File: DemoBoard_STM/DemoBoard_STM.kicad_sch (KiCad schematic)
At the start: 56 parts, among them J1 USB4110GFA, J6 M55-7101242R, J7 MSD-1-A, J8 Conn_01x17_Pin, SW1 SW_Push, SW2 SW_Push, U1 RP2040, U2 W25Q128JVSIM, U3 MCP2518FDT-E_QBB, U4 TCAN332DCNR, U5 TLV75533PDBVR, Y1 ABM8-272-T3, Y2 ABM8-20.000MHZ-10-B1U-T

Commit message: Implement STM schematic
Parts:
- removed C1, C2: 15pF, Capacitor_SMD:C_0402_1005Metric_Pad0.74x0.62mm_HandSolder, symbol Device:C
- removed C10, C11, C13, C4, C5, C6, C7, C8: 100nF, Capacitor_SMD:C_0402_1005Metric_Pad0.74x0.62mm_HandSolder, symbol Device:C
- removed C3, C9: 1uF, Capacitor_SMD:C_0402_1005Metric_Pad0.74x0.62mm_HandSolder, symbol Device:C
- removed R2, R4: 27.4, Resistor_SMD:R_0402_1005Metric_Pad0.72x0.64mm_HandSolder, symbol Device:R_US
- removed R3: 10k, Resistor_SMD:R_0402_1005Metric_Pad0.72x0.64mm_HandSolder, symbol Device:R_US
- removed R5: 1k, Resistor_SMD:R_0402_1005Metric_Pad0.72x0.64mm_HandSolder, symbol Device:R_US
- removed TP1: 1.2V, TestPoint:TestPoint_Pad_D1.0mm, symbol Connector:TestPoint
- removed TP3: 3.3V, TestPoint:TestPoint_Pad_D1.0mm, symbol Connector:TestPoint
- removed U1: RP2040, Package_DFN_QFN:QFN-56-1EP_7x7mm_P0.4mm_EP3.2x3.2mm, symbol MCU_RaspberryPi:RP2040
- removed Y1: ABM8-272-T3, inspireFly:XTAL_ABM8-272-T3, symbol inspireFly:ABM8-272-T3
- added C26, C40: 1uF, Capacitor_SMD:C_0402_1005Metric_Pad0.74x0.62mm_HandSolder, symbol Device:C
- added C27, C28, C29, C31, C35, C36, C37, C38, C39, C41: 100nF, Capacitor_SMD:C_0402_1005Metric_Pad0.74x0.62mm_HandSolder, symbol Device:C
- added C30, C32: 10uF, Capacitor_SMD:C_0402_1005Metric_Pad0.74x0.62mm_HandSolder, symbol Device:C
- added C33, C34: 2.2uF, Capacitor_SMD:C_0402_1005Metric_Pad0.74x0.62mm_HandSolder, symbol Device:C
- added D3: PESD3V3U1UL, Diode_SMD:D_SOD-882, symbol Diode:PESD3V3U1UL
- added D4, D5: ESDA14V2SC5, Package_TO_SOT_SMD:SOT-23-5, symbol Power_Protection:ESDA14V2SC5
- added J2: Conn_ST_STDC14, symbol Connector:Conn_ST_STDC14
- added L1: 2.2uH, Inductor_SMD:L_0402_1005Metric_Pad0.77x0.64mm_HandSolder, symbol Device:L
- added U1: STM32U375CGT6Q, inspireFly:LQFP48_STM, symbol STM32U375:STM32U375CGT6Q
- added Y1: 32.768kHz, Crystal:Crystal_SMD_2012-2Pin_2.0x1.2mm_HandSoldering, symbol Device:Crystal
- added Y3: 16MHz, Crystal:Crystal_SMD_3225-4Pin_3.2x2.5mm_HandSoldering, symbol Device:Crystal_GND24
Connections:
- net RESET is gone; now on net COVER_GND: SW1.1
- net COVER_GND: now also C26.1, C27.1, C28.1, C29.1, C30.1, C31.1, C32.2, C33.1, C34.2, C35.2, C36.1, C37.2, C38.2, C39.2, C40.2, C41.1, D3.2 (A), D4.2 (A), D5.2 (A), J2.11 (GNDDetect), J2.5 (GND), J2.7 (GND), J2.9 (JRCLK/NC), U1.22 (VSSSMPS), U1.24 (VSS), U1.35 (VSS), U1.47 (VSS), U1.8 (VSSA), Y3.2 (G), Y3.4 (G); no longer SW1.2
- new net: C37.1, U1.6 (PH1-OSC_OUT), Y3.1
- new net: D4.5 (K), J2.10 (JTDI/NC), U1.38 (PA15)
- new net: C41.2, D3.1 (K), D5.1 (K), J2.12 (~{RST}), SW1.2, U1.7 (NRST)
- new net: D5.5 (K), J2.13 (VCP_RX), U1.31 (PA10)
- new net: D5.4 (K), J2.14 (VCP_TX), U1.30 (PA9)
- new net: D4.1 (K), J2.4 (JTMS/SWDIO), U1.34 (PA13)
- new net: D4.3 (K), J2.6 (JCLK/SWCLK), U1.37 (PA14)
- new net: D4.4 (K), J2.8 (JTDO/SWO), U1.39 (PB3)
- new net: L1.1, U1.20 (VLXSMPS)
- new net: C33.2, C34.1, L1.2, U1.23 (VDD11), U1.46 (VDD11)
- new net: C38.1, U1.5 (PH0-OSC_IN), Y3.3
- new net: C35.1, U1.3 (PC14-OSC32_IN), Y1.2
- new net: C36.2, U1.4 (PC15-OSC32_OUT), Y1.1
- new net PA0: U1.10 (PA0)
- new net PA1: U1.11 (PA1)
- new net PA11: U1.32 (PA11)
- new net PA12: U1.33 (PA12)
- new net PA2: U1.12 (PA2)
- new net PA3: U1.13 (PA3)
- new net PA4: U1.14 (PA4)
- new net PA5: U1.15 (PA5)
- new net PA6: U1.16 (PA6)
- new net PA7: U1.17 (PA7)
- new net PA8: U1.29 (PA8)
- new net PB0: U1.18 (PB0)
- new net PB1: U1.19 (PB1)
- new net PB13: U1.26 (PB13)
- new net PB14: U1.27 (PB14)
- new net PB15: U1.28 (PB15)
- new net PB4: U1.40 (PB4)
- new net PB5: U1.41 (PB5)
- new net PB6: U1.42 (PB6)
- new net PB7: U1.43 (PB7)
- new net PB8: U1.45 (PB8)
- new net PC13: U1.2 (PC13)
- new net PH3-BOOT0: U1.44 (PH3-BOOT0)
- new net VBAT: C26.2, U1.1 (VBAT)
- new net VCC: J2.3 (VCC)
- new net VDD: C27.2, C28.2, C29.2, C30.2, C31.2, C32.1, U1.21 (VDDSMPS), U1.25 (VDD), U1.36 (VDD), U1.48 (VDD)
- new net VDDA: C39.1, C40.1, U1.9 (VDDA)
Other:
- note added: "STM32U375CGT6Q"
- note removed: "Ground unused ADC pins"
- note removed: "Integration References: https://pip-assets.raspberrypi.com/categories/814-rp2040/documents/RP-008279-DS-1-hardware-design-with-rp2040.pdf?disposition=inline https://pip-assets.raspberrypi.com/categories/610-raspberry-pi-pico/documents/RP-008307-DS-1-pico-datasheet.pdf?disposition=inline#pico-schematic-diagram"
- note removed: "Place 27.4 ohm near respective pins"
- note removed: "Place C3/1uF near pin 45"
- note removed: "Place C9/1uF near pin 44"
- note removed: "RP2040"

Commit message: Fix cap values for clock
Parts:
- C35, C36: value 100nF -> 6.8pF
- C37, C38: value 100nF -> 12pF
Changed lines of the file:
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@@
 			)
 		)
-		(property "Value" "100nF"
+		(property "Value" "12pF"
 			(at 173.99 60.706 0)
 			(show_name no)
@@
 			)
 		)
-		(property "Value" "100nF"
+		(property "Value" "6.8pF"
 			(at 172.72 43.434 0)
 			(show_name no)
@@
 			)
 		)
-		(property "Value" "100nF"
+		(property "Value" "6.8pF"
 			(at 175.26 27.686 0)
 			(show_name no)
@@
 			)
 		)
-		(property "Value" "100nF"
+		(property "Value" "12pF"
 			(at 162.56 50.546 0)
 			(show_name no)

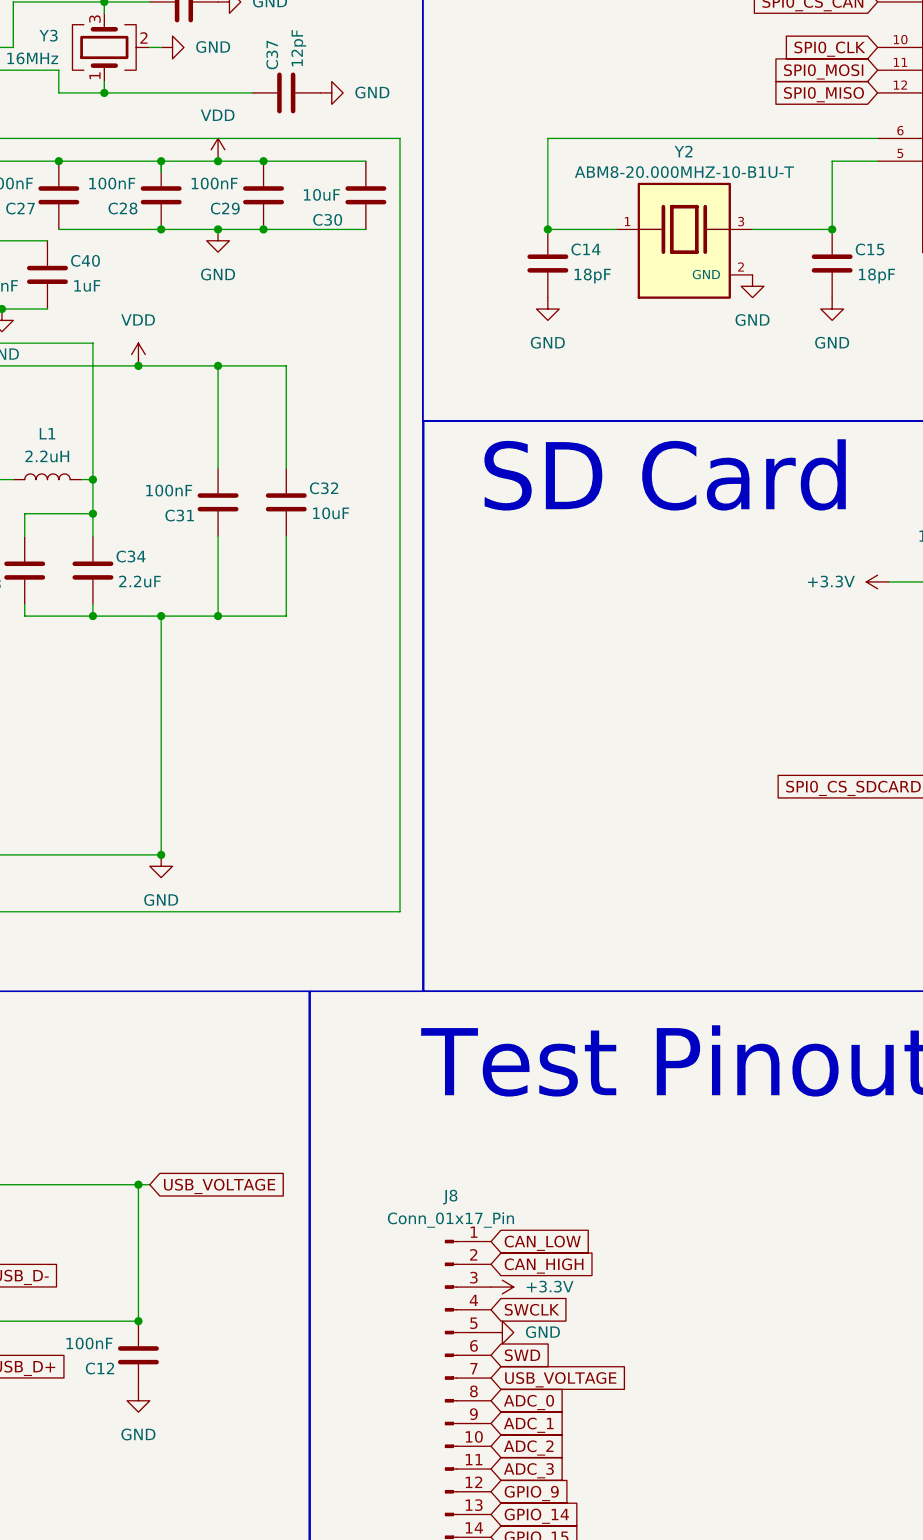
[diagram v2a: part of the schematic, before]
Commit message: Routed capacitors
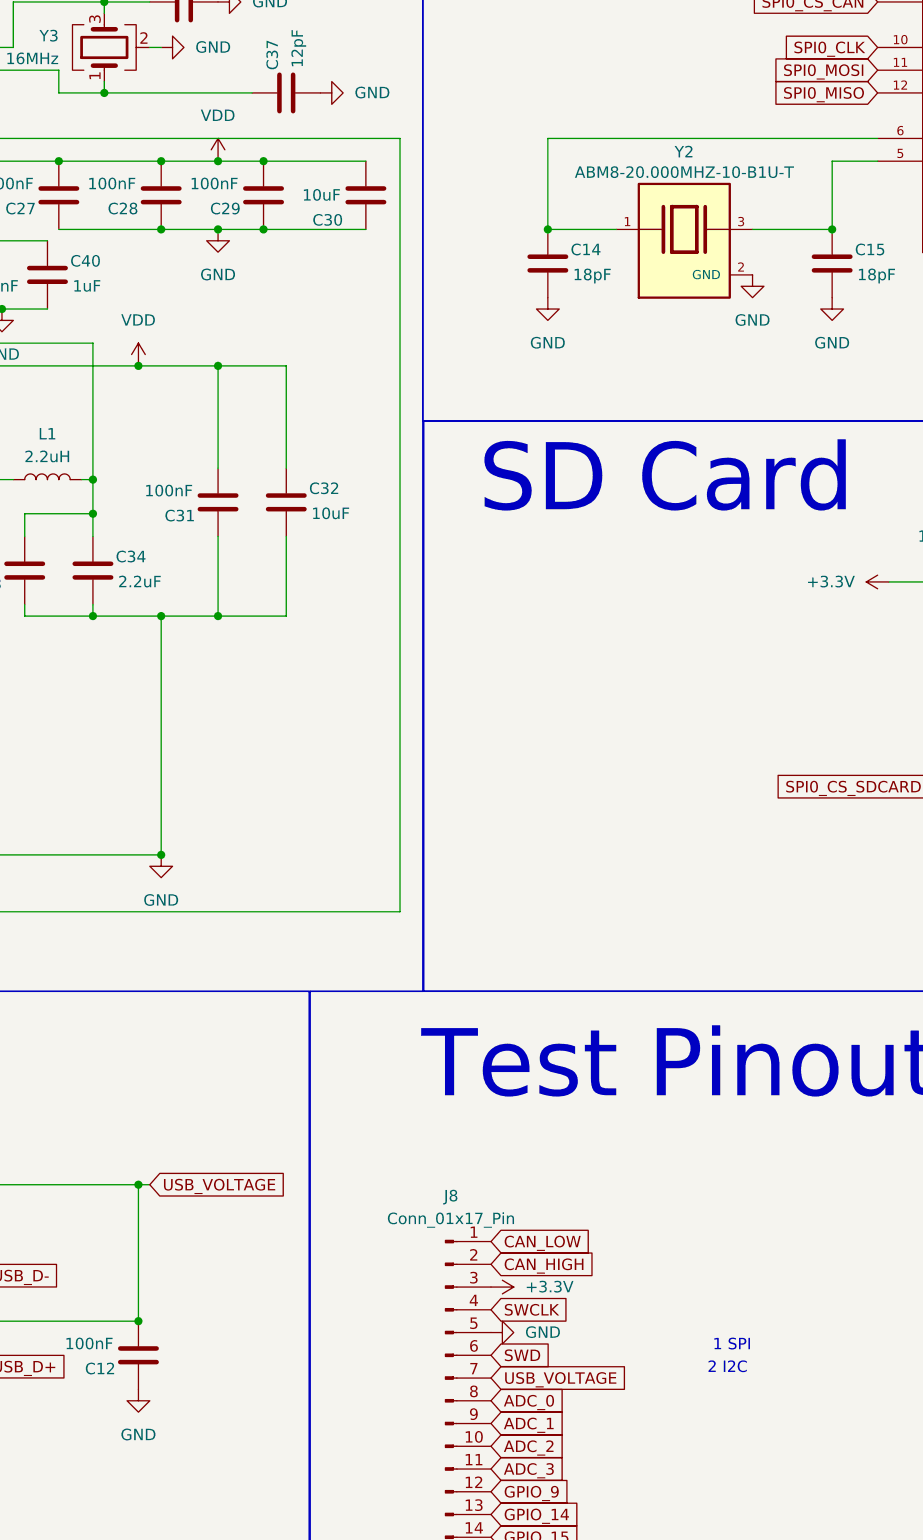
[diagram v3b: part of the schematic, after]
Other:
- note added: "1 SPI"
- note added: "2 I2C"

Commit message: Routing + schematic updates for STM
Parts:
- removed C12, C17, C41: 100nF, Capacitor_SMD:C_0402_1005Metric_Pad0.74x0.62mm_HandSolder, symbol Device:C
- removed C14, C15: 18pF, Capacitor_SMD:C_0402_1005Metric_Pad0.74x0.62mm_HandSolder, symbol Device:C
- removed C26: 1uF, Capacitor_SMD:C_0402_1005Metric_Pad0.74x0.62mm_HandSolder, symbol Device:C
- removed CR1: USBLC6-2SC6, Package_TO_SOT_SMD:SOT-23-6, symbol inspireFly:USBLC6-2SC6
- removed D1: LTST-C190KSKT, LED_SMD:LED_0603_1608Metric_Pad1.05x0.95mm_HandSolder, symbol Device:LED
- removed D2: LTST-S270KRKT, LED_SMD:LED_0603_1608Metric_Pad1.05x0.95mm_HandSolder, symbol Device:LED
- removed D3: PESD3V3U1UL, Diode_SMD:D_SOD-882, symbol Diode:PESD3V3U1UL
- removed D4, D5: ESDA14V2SC5, Package_TO_SOT_SMD:SOT-23-5, symbol Power_Protection:ESDA14V2SC5
- removed R8, R9: 1k, Resistor_SMD:R_0402_1005Metric_Pad0.72x0.64mm_HandSolder, symbol Device:R_US
- removed U2: W25Q128JVSIM, inspireFly:SOIC_128JVSIM_WIN, symbol inspireFly:W25Q128JVSIM
- removed U3: MCP2518FDT-E_QBB, inspireFly:SON65P450X300X90-15N, symbol inspireFly:MCP2518FDT-E_QBB
- removed Y2: ABM8-20.000MHZ-10-B1U-T, inspireFly:XTAL_ABM8-272-T3, symbol inspireFly:ABM8-272-T3
- removed Y3: 16MHz, Crystal:Crystal_SMD_3225-4Pin_3.2x2.5mm_HandSoldering, symbol Device:Crystal_GND24
- added CR1, CR2: ESDA14V2SC6, inspireFly:SOT23-6_1P75X3P05X0P95_STM, symbol inspireFly:ESDA14V2SC6
- added R12: 10k, Resistor_SMD:R_0402_1005Metric_Pad0.72x0.64mm_HandSolder, symbol Device:R_US
- added R13: 100k, Resistor_SMD:R_0402_1005Metric_Pad0.72x0.64mm_HandSolder, symbol Device:R_US
- added U3: W25Q128JVPIQ TR, inspireFly:WSON-8_6X5_WIN, symbol inspireFly:W25Q128JVPIQ_TR
- added Y2: 8Z-16.000MAHE-T, Crystal:Crystal_SMD_2520-4Pin_2.5x2.0mm, symbol Device:Crystal_GND24
- C35, C36: value 6.8pF -> 22pF
- C37, C38: value 12pF -> 18pF
- J2: footprint (none) -> inspireFly:SAMTEC_FTSH-107-01-L-DV-K-A
- L1: footprint Inductor_SMD:L_0402_1005Metric_Pad0.77x0.64mm_HandSolder -> inspireFly:INDC1608X95N
- Y1: footprint Crystal:Crystal_SMD_2012-2Pin_2.0x1.2mm_HandSoldering -> inspireFly:XTAL_ABS07-32.768KHZ-T
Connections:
- net GPIO_16 is gone; now on net CAN_HIGH: J8.15 (Pin_15)
- net GPIO_17 is gone; now on net CAN_LOW: J8.16 (Pin_16)
- net PA11 is gone; now on net CAN_RX: U1.32 (PA11)
- net PA12 is gone; now on net CAN_TX: U1.33 (PA12)
- net PA2 is gone; now on net QSPI_CS: U1.12 (PA2)
- net PA3 is gone; now on net QSPI_CLK: U1.13 (PA3)
- net PA6 is gone; now on net QSPI_SD3: U1.16 (PA6)
- net PA7 is gone; now on net QSPI_SD2: U1.17 (PA7)
- net PA8 is gone; now on net SPI2_CS2: U1.29 (PA8)
- net PB0 is gone; now on net QSPI_SD1: U1.18 (PB0)
- net PB1 is gone; now on net QSPI_SD0: U1.19 (PB1)
- net PB13 is gone; now on net SPI2_CLK: U1.26 (PB13)
- net PB14 is gone; now on net SPI2_MISO: U1.27 (PB14)
- net PB15 is gone; now on net SPI2_MOSI: U1.28 (PB15)
- net PB6 is gone; now on net I2C1_SCL: U1.42 (PB6)
- net PB7 is gone; now on net I2C1_SDA: U1.43 (PB7)
- net PB8 is gone; now on net SPI2_CS1: U1.45 (PB8)
- net SPI0_CLK is gone; now on net SPI1_CLK: J7.5 (CLK)
- net SPI0_CS_SDCARD is gone; now on net SPI1_CS_SDCARD: J7.2 (CD/DAT3), R11.2
- net SPI0_MISO is gone; now on net SPI1_MISO: J7.7 (DAT0)
- net SPI0_MOSI is gone; now on net SPI1_MOSI: J7.3 (CMD)
- net SWCLK is gone; now on net COVER_GND: J8.4 (Pin_4)
- net SWD is gone; now on net ADC1_IN4: J8.6 (Pin_6)
- net VBAT is gone; now on net +3.3V: U1.1 (VBAT)
- net VCC is gone; now on net +3.3V: J2.3 (VCC)
- net VDD is gone; now on net +3.3V: C27.2, C28.2, C29.2, C30.2, C31.2, C32.1, U1.21 (VDDSMPS), U1.25 (VDD), U1.36 (VDD), U1.48 (VDD)
- net VDDA is gone; now on net +3.3V: C39.1, C40.1, U1.9 (VDDA)
- net +3.3V: now also J8.1 (Pin_1), J8.2 (Pin_2), R7.2, SW2.2, CR1.1, R12.1, U3.8 (VCC); no longer J8.3 (Pin_3)
- net CAN_HIGH: no longer J8.2 (Pin_2)
- net CAN_LOW: no longer J8.1 (Pin_1)
- net COVER_GND: now also C38.1, J8.3 (Pin_3), CR1.2, CR1.5, CR2.2, CR2.5, R13.2, U3.4 (GND), U3.9 (GND), Y2.2 (G), Y2.4 (G); no longer C38.2, J2.9 (JRCLK/NC), SW2.1
- net PH3-BOOT0: now also SW2.1, R13.1
- net QSPI_CLK: now also U3.6 (CLK)
- net QSPI_CS: now also U3.1 (/CS)
- net QSPI_SD0: now also U3.5 (DI(IO0))
- net QSPI_SD1: now also U3.2 (DO(IO1))
- net QSPI_SD2: now also U3.3 (/WP(IO2))
- net QSPI_SD3: now also U3.7 (/HOLD_/RESET)
- net VBUS: no longer J8.7 (Pin_7)
- net CAN_TX: now reaches U4.1 (TXD)
- net CAN_RX: now reaches U4.4 (RXD)
- net at C37.1, U1.6 (PH1-OSC_OUT): now also Y2.3
- net at J1.A7 (DN1): no longer J1.B7 (DN2)
- net at J1.A6 (DP1): no longer J1.B6 (DP2)
- net JTDI: now reaches J2.10 (JTDI/NC), U1.38 (PA15)
- net JTDI: now also CR2.3
- net NRST: now reaches J2.12 (~{RST}), SW1.2, U1.7 (NRST)
- net NRST: now also CR1.6, R12.2
- net DEBUG_LPUART_RX: now reaches U1.31 (PA10)
- net DEBUG_LPUART_RX: now also J2.14 (VCP_TX), CR1.3; no longer J2.13 (VCP_RX)
- net DEBUG_LPUART_TX: now reaches U1.30 (PA9)
- net DEBUG_LPUART_TX: now also J2.13 (VCP_RX), CR1.4; no longer J2.14 (VCP_TX)
- net JTMS/SWDIO: now reaches J2.4 (JTMS/SWDIO), U1.34 (PA13)
- net JTMS/SWDIO: now also CR2.4
- net JTCK/SWCLK: now reaches J2.6 (JCLK/SWCLK), U1.37 (PA14)
- net JTCK/SWCLK: now also CR2.6
- net SWO: now reaches J2.8 (JTDO/SWO), U1.39 (PB3)
- net SWO: now also CR2.1
- net +1.1V: now reaches C33.2, C34.1, L1.2, U1.23 (VDD11), U1.46 (VDD11)
- net at U1.5 (PH0-OSC_IN): now also C38.2, Y2.1; no longer C38.1
- net ADC_0 renamed SPI2_CS1
- net ADC_1 renamed SPI2_CS2
- net ADC_2 renamed SPI2_CLK
- net ADC_3 renamed SPI2_MOSI
- net GPIO_14 renamed I2C1_SDA
- net GPIO_15 renamed I2C1_SCL
- net GPIO_9 renamed SPI2_MISO
- net PA0 renamed ADC1_IN3
- net ADC1_IN3: now also J8.7 (Pin_7)
- net PA1 renamed ADC1_IN4
- net PA4 renamed SPI1_CS_SDCARD
- net PA5 renamed SPI1_CLK
- net PB4 renamed SPI1_MISO
- net PB5 renamed SPI1_MOSI
- net PC13: no longer names the net of U1.2 (PC13)
- no-connect marks 8 -> 11
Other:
- note added: "CAN Transceiver"
- note removed: "1 SPI"
- note removed: "2 I2C"
- note removed: "CAN Controller + Transceiver"
- note removed: "Debug LEDs"
- note removed: "Red"
- note removed: "Yellow"
- moved on the sheet: C16, C18, C19, C20, C21, C22, C23, C25, C35, C36, J2, J6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
